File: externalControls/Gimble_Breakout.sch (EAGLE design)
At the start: 5 parts

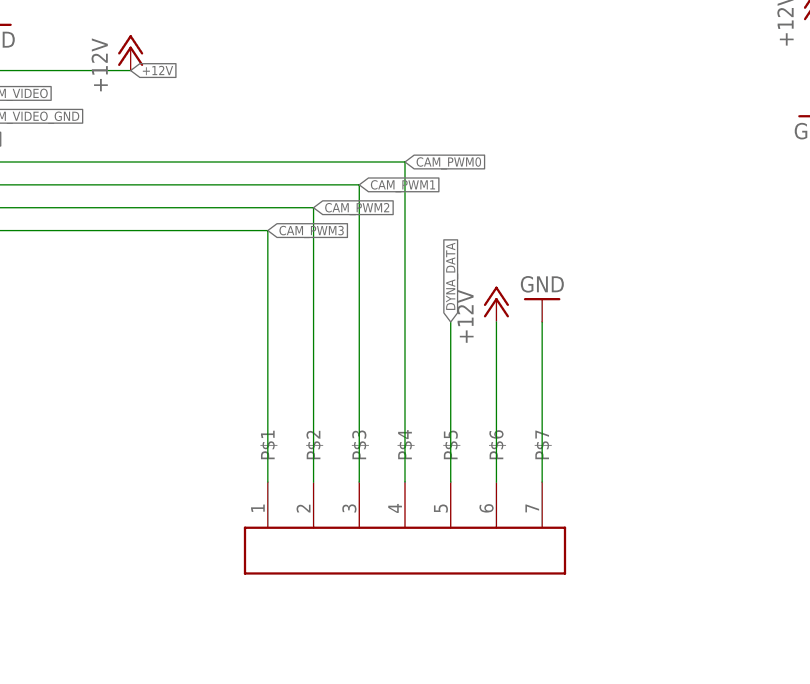
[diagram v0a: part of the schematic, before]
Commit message: Updated Routing
optimized a few paths
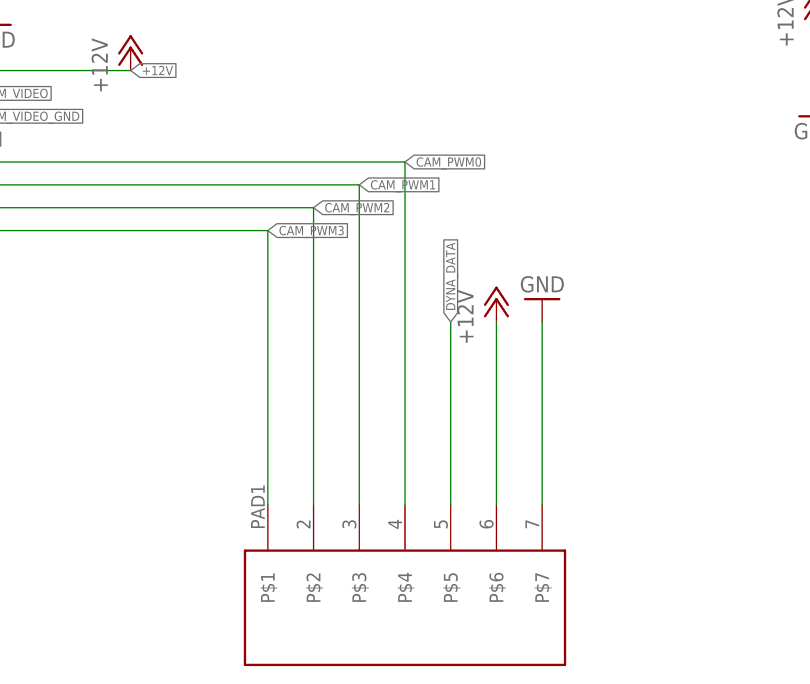
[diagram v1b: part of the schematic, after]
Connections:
- net +12V: now also U$2.P$6
- net CAM_PWM0: now also U$2.P$4
- net CAM_PWM1: now also U$2.P$3
- net CAM_PWM2: now also U$2.P$2
- net CAM_PWM3: now also U$2.P$1
- net DYNA_DATA: now also U$2.P$5
- net GND: now also U$2.P$7
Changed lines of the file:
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@@
 <instance part="P+1" gate="1" x="236.22" y="299.72"/>
 <instance part="U$1" gate="G$1" x="162.56" y="332.74"/>
-<instance part="U$2" gate="G$1" x="172.72" y="241.3" rot="R270"/>
+<instance part="U$2" gate="G$1" x="172.72" y="238.76" rot="R270"/>
 <instance part="P+3" gate="1" x="160.02" y="294.64"/>
 <instance part="GND2" gate="1" x="144.78" y="297.18"/>
@@
 </segment>
 <segment>
-<wire x1="205.74" y1="246.38" x2="205.74" y2="264.16" width="0.1524" layer="91"/>
+<wire x1="205.74" y1="243.84" x2="205.74" y2="264.16" width="0.1524" layer="91"/>
 <pinref part="GND3" gate="1" pin="GND"/>
+<pinref part="U$2" gate="G$1" pin="P$7"/>
 </segment>
 </net>
@@
 </segment>
 <segment>
-<wire x1="200.66" y1="246.38" x2="200.66" y2="264.16" width="0.1524" layer="91"/>
+<wire x1="200.66" y1="243.84" x2="200.66" y2="264.16" width="0.1524" layer="91"/>
 <pinref part="P+4" gate="1" pin="+12V"/>
+<pinref part="U$2" gate="G$1" pin="P$6"/>
 </segment>
 </net>
@@
 </segment>
 <segment>
-<wire x1="195.58" y1="246.38" x2="195.58" y2="264.16" width="0.1524" layer="91"/>
+<wire x1="195.58" y1="243.84" x2="195.58" y2="264.16" width="0.1524" layer="91"/>
 <label x="195.58" y="264.16" size="1.016" layer="95" rot="R90" xref="yes"/>
+<pinref part="U$2" gate="G$1" pin="P$5"/>
 </segment>
 </net>
@@
 <label x="175.26" y="274.32" size="1.016" layer="95" xref="yes"/>
 <wire x1="132.08" y1="274.32" x2="175.26" y2="274.32" width="0.1524" layer="91"/>
-<wire x1="175.26" y1="274.32" x2="175.26" y2="246.38" width="0.1524" layer="91"/>
+<wire x1="175.26" y1="274.32" x2="175.26" y2="243.84" width="0.1524" layer="91"/>
+<pinref part="U$2" gate="G$1" pin="P$1"/>
 </segment>
 </net>
@@
 <label x="180.34" y="276.86" size="1.016" layer="95" xref="yes"/>
 <wire x1="132.08" y1="276.86" x2="180.34" y2="276.86" width="0.1524" layer="91"/>
-<wire x1="180.34" y1="276.86" x2="180.34" y2="246.38" width="0.1524" layer="91"/>
+<wire x1="180.34" y1="276.86" x2="180.34" y2="243.84" width="0.1524" layer="91"/>
+<pinref part="U$2" gate="G$1" pin="P$2"/>
 </segment>
 </net>
@@
 <label x="185.42" y="279.4" size="1.016" layer="95" xref="yes"/>
 <wire x1="132.08" y1="279.4" x2="185.42" y2="279.4" width="0.1524" layer="91"/>
-<wire x1="185.42" y1="279.4" x2="185.42" y2="246.38" width="0.1524" layer="91"/>
+<wire x1="185.42" y1="279.4" x2="185.42" y2="243.84" width="0.1524" layer="91"/>
+<pinref part="U$2" gate="G$1" pin="P$3"/>
 </segment>
 </net>
@@
 <pinref part="SV1" gate="G$1" pin="4"/>
 <wire x1="132.08" y1="281.94" x2="190.5" y2="281.94" width="0.1524" layer="91"/>
-<wire x1="190.5" y1="281.94" x2="190.5" y2="246.38" width="0.1524" layer="91"/>
+<wire x1="190.5" y1="281.94" x2="190.5" y2="243.84" width="0.1524" layer="91"/>
+<pinref part="U$2" gate="G$1" pin="P$4"/>
 </segment>
 </net>
